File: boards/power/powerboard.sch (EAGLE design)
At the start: 55 parts, among them IC1 TPS5420, IC2 TPS5420

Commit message: Changing boards for fet and text improvements
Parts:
- R2, R4: value (none) -> 500
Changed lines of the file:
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@@
 <part name="R6" library="rcl" deviceset="R-TRIMM" device="3224W"/>
 <part name="R7" library="rcl" deviceset="R-TRIMM" device="3224W"/>
-<part name="R2" library="rcl" deviceset="R-US_" device="R3216"/>
-<part name="R4" library="rcl" deviceset="R-US_" device="R3216"/>
+<part name="R2" library="rcl" deviceset="R-US_" device="R3216" value="500"/>
+<part name="R4" library="rcl" deviceset="R-US_" device="R3216" value="500"/>
 <part name="U$2" library="40xx" deviceset="LM3488" device=""/>
 <part name="COUT" library="rcl" deviceset="CPOL-EU" device="SANYO_SMD_A5" value="56uF"/>

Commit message: New board for plugin regulator
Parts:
- removed CBP: 100nF, rcl:C-EUC0805
- removed CCOMP: 120nF, rcl:C-EUC0805
- removed CCOMP2: 510pF, rcl:C-EUC0805
- removed CIN: 22uF, rcl:C-EUC0805
- removed COUT, COUT1: 56uF, rcl:CPOL-EUSANYO_SMD_A5
- removed CRAMP: 750pF, rcl:C-EUC0805
- removed CSEP: 2.2uF, rcl:C-EUC0805
- removed LIN: 6.2uH, SparkFun-Passives:INDUCTORSRU1038
- removed LOUT: 15uH, SparkFun-Passives:INDUCTORSRU1038
- removed RBP: 20.0, rcl:R-US_R0805
- removed RCOMP: 1.47k, rcl:R-US_R0805
- removed RFADJ: 34.8k, rcl:R-US_R0805
- removed RFB1: 10k, rcl:R-US_R0805
- removed RFB2: 37.4k, rcl:R-US_R0805
- removed RRAMP: 100.0, rcl:R-US_R0805
- removed RSENSE: 0.016, rcl:R-EU_R2512
- removed U$5: P-CHANNEL20V(D-S)MOSFET, ngohara_parts:P-CHANNEL20V(D-S)MOSFET
- removed U$6: DPAK_DIODE, ngohara_parts:DPAK_DIODE
- added JP1: (no value), SparkFun-Connectors:M04LOCK
- added R10, R11, R8, R9: 0, resistor:R-EU_R0805
- added U$4: THERMAL_PAD, ngohara_parts:THERMAL_PAD
- U$2: value LM3488 -> THERMAL_PAD; device 40xx:LM3488 -> ngohara_parts:THERMAL_PAD
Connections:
- removed net 6V: COUT.+, COUT1.+, RFB2.1, U$6.C, X3.2
- removed net FB: RFB1.1, RFB2.2, U$2.FB
- removed net LINSIG: CSEP.1, LIN.2, U$5.S
- removed net LSIG: CSEP.2, LOUT.1, U$6.A
- removed net N$1: CCOMP.1, RCOMP.1
- removed net N$20: RFADJ.2, U$2.FA/SD
- removed net N$21: CRAMP.1, RRAMP.2, U$2.ISEN
- removed net N$23: U$2.DR, U$5.G
- removed net N$3: CCOMP2.1, RCOMP.2, U$2.COMP
- removed net N$9: CBP.1, RBP.1, U$2.VIN
- removed net SIG1: RRAMP.1, RSENSE.2, U$5.D
- new net 6VOUT: JP1.4, X3.2
- new net VIN: JP1.2, R10.2, R11.2, R8.2, R9.2
- net 5V: now also R10.1, R11.1
- net GND: now also JP1.3; no longer CBP.2, CCOMP.2, CCOMP2.2, CIN.2, COUT.-, COUT1.-, CRAMP.2, LOUT.2, RFADJ.1, RFB1.2, RSENSE.1, U$2.AGND, U$2.PGND
- net V_BATT: now also R8.1, R9.1; no longer CIN.1, LIN.1, RBP.2
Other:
- moved on the sheet: X3

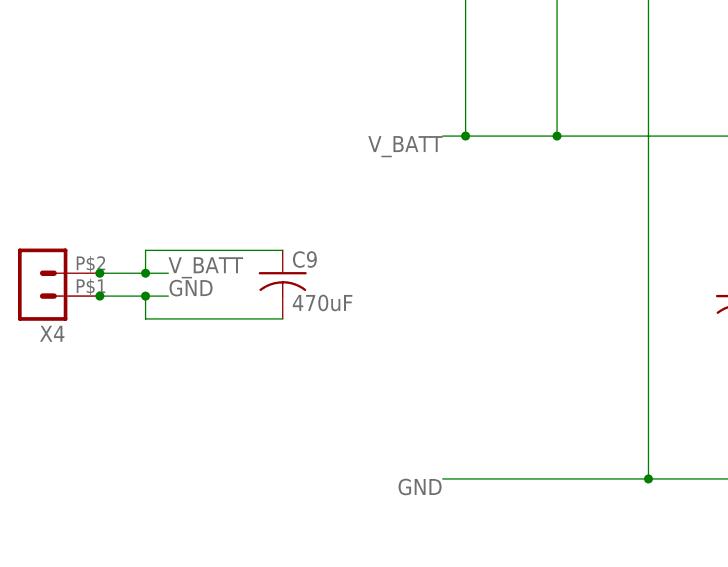
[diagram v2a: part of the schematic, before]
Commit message: Fixed 470 cap footprint
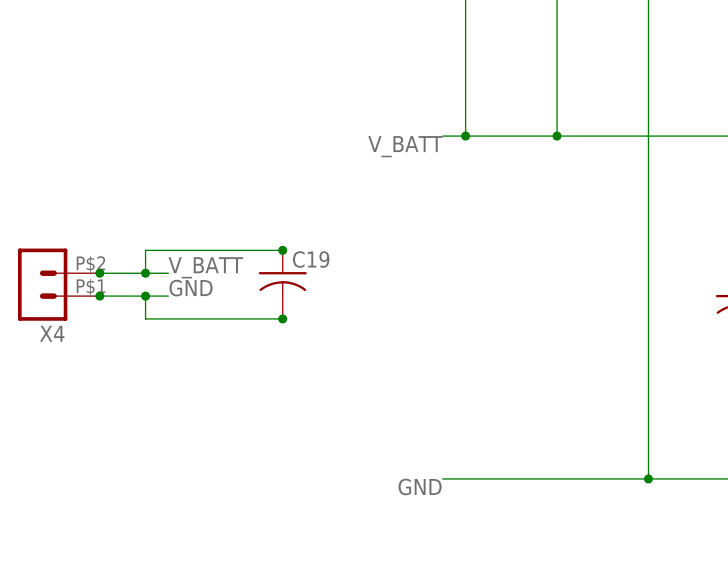
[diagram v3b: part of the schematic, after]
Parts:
- removed C9: 470uF, resistor:C-USC1812K
- added C19: (no value), custom_cap:C-USC2220K
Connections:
- net GND: now also C19.2; no longer C9.2
- net V_BATT: now also C19.1; no longer C9.1
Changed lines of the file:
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@@
 <?xml version="1.0" encoding="utf-8"?>
 <!DOCTYPE eagle SYSTEM "eagle.dtd">
-<eagle version="6.4">
+<eagle version="6.5.0">
 <drawing>
 <settings>
@@
 <part name="U$1" library="inductor-coilcraft-3" deviceset="MSS1260" device="" value="33uH"/>
 <part name="IC1" library="daniel" deviceset="TPS5420" device=""/>
-<part name="C9" library="resistor" deviceset="C-US" device="C1812K" value="470uF"/>
 <part name="C10" library="rcl" deviceset="CPOL-US" device="C/6032-28R" value="100uF"/>
 <part name="C11" library="rcl" deviceset="C-US" device="C1206K" value=".1uF"/>
@@
 <part name="U$2" library="ngohara_parts" deviceset="THERMAL_PAD" device=""/>
 <part name="U$4" library="ngohara_parts" deviceset="THERMAL_PAD" device=""/>
+<part name="C19" library="custom_cap" deviceset="C-US" device="C2220K"/>
 </parts>
 <sheets>
@@
 <instance part="U$1" gate="G$1" x="53.34" y="-20.32" rot="R90"/>
 <instance part="IC1" gate="P" x="20.32" y="-25.4"/>
-<instance part="C9" gate="G$1" x="-68.58" y="-35.56"/>
 <instance part="C10" gate="G$1" x="96.52" y="27.94"/>
 <instance part="C11" gate="G$1" x="109.22" y="27.94"/>
@@
 <instance part="U$2" gate="G$1" x="10.16" y="-99.06"/>
 <instance part="U$4" gate="G$1" x="10.16" y="-114.3"/>
+<instance part="C19" gate="G$1" x="-68.58" y="-35.56"/>
 </instances>
 <busses>
@@
 <junction x="-83.82" y="-38.1"/>
 <wire x1="-83.82" y1="-38.1" x2="-83.82" y2="-40.64" width="0.1524" layer="91"/>
-<pinref part="C9" gate="G$1" pin="2"/>
 <wire x1="-68.58" y1="-40.64" x2="-83.82" y2="-40.64" width="0.1524" layer="91"/>
 <label x="-81.28" y="-38.1" size="1.778" layer="95"/>
+<pinref part="C19" gate="G$1" pin="2"/>
+<junction x="-68.58" y="-40.64"/>
 </segment>
 <segment>
@@
 <wire x1="-81.28" y1="-35.56" x2="-83.82" y2="-35.56" width="0.1524" layer="91"/>
 <wire x1="-83.82" y1="-35.56" x2="-83.82" y2="-33.02" width="0.1524" layer="91"/>
-<pinref part="C9" gate="G$1" pin="1"/>
 <wire x1="-68.58" y1="-33.02" x2="-83.82" y2="-33.02" width="0.1524" layer="91"/>
 <label x="-81.28" y="-35.56" size="1.778" layer="95"/>
+<pinref part="C19" gate="G$1" pin="1"/>
+<junction x="-68.58" y="-33.02"/>
 </segment>
 </net>

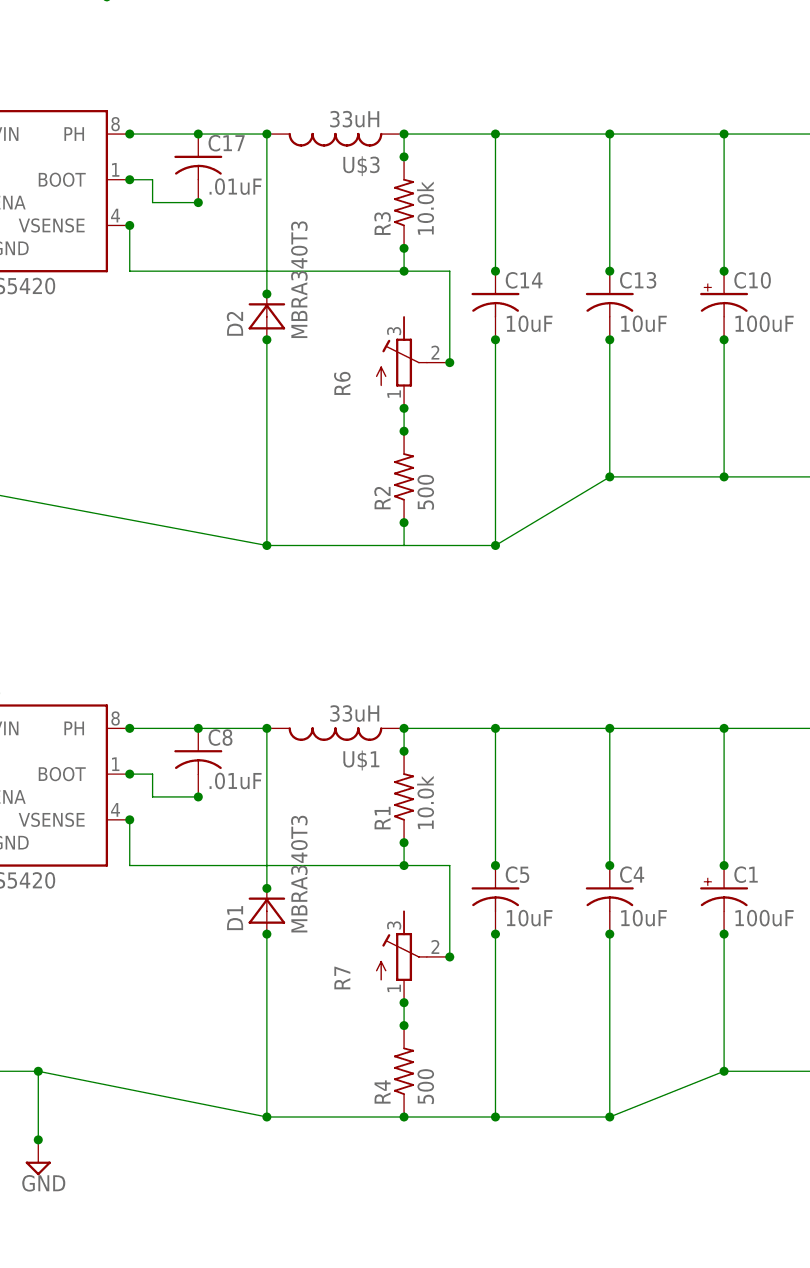
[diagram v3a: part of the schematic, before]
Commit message: changed resistors and fixed text
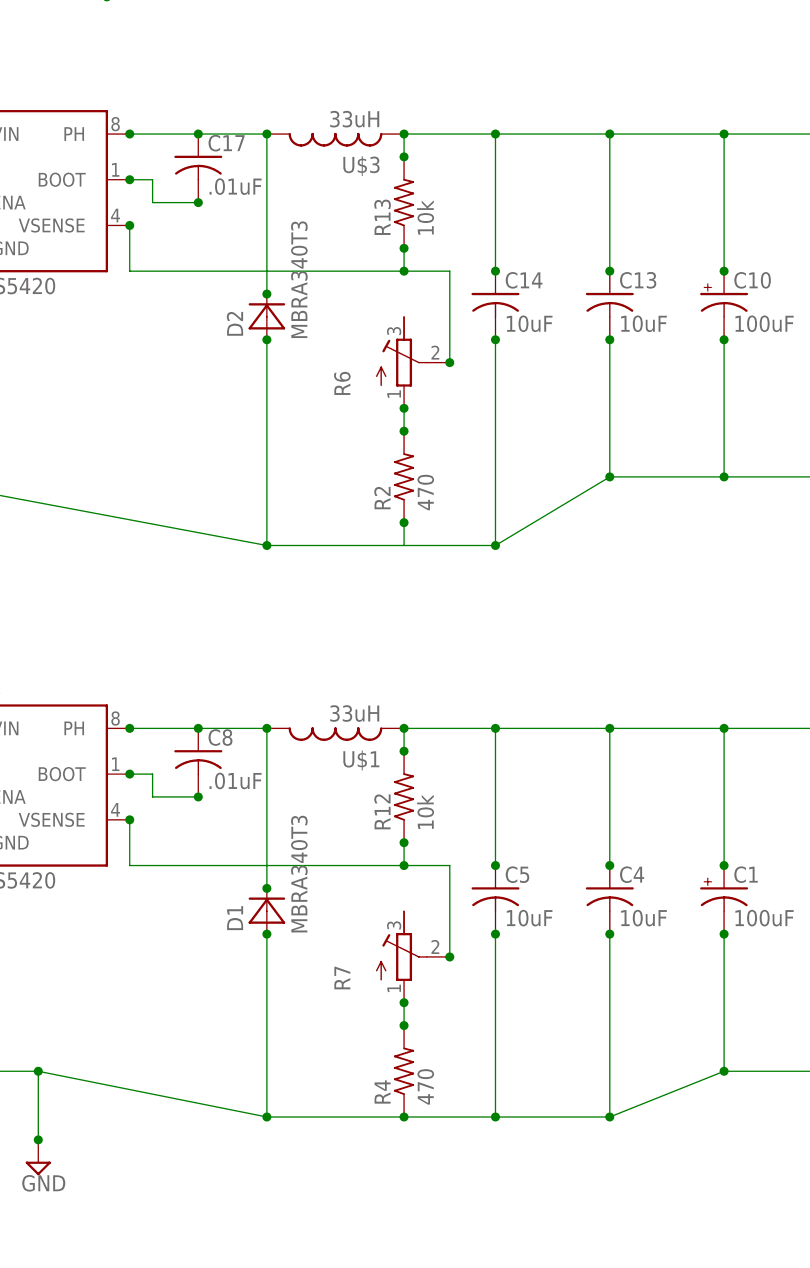
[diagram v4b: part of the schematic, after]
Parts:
- removed R1, R3: 10.0k, rcl:R-US_R3216
- added R12, R13: 10k, rcl:R-US_M0805
- R2, R4: value 500 -> 470
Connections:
- net 3_3V: now also R13.2; no longer R3.2
- net 5V: now also R12.2; no longer R1.2
- net N$12: now also R13.1; no longer R3.1
- net N$5: now also R12.1; no longer R1.1
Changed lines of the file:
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@@
 <part name="D1" library="diode" deviceset="MBRA340T3" device=""/>
 <part name="C8" library="rcl" deviceset="C-US" device="C0805K" value=".01uF"/>
-<part name="R1" library="rcl" deviceset="R-US_" device="R3216" value="10.0k"/>
 <part name="SUPPLY1" library="supply2" deviceset="GND" device=""/>
 <part name="U$1" library="inductor-coilcraft-3" deviceset="MSS1260" device="" value="33uH"/>
@@
 <part name="D2" library="diode" deviceset="MBRA340T3" device=""/>
 <part name="C17" library="rcl" deviceset="C-US" device="C0805K" value=".01uF"/>
-<part name="R3" library="rcl" deviceset="R-US_" device="R3216" value="10.0k"/>
 <part name="U$3" library="inductor-coilcraft-3" deviceset="MSS1260" device="" value="33uH"/>
 <part name="IC2" library="daniel" deviceset="TPS5420" device=""/>
@@
 <part name="R6" library="rcl" deviceset="R-TRIMM" device="3224W"/>
 <part name="R7" library="rcl" deviceset="R-TRIMM" device="3224W"/>
-<part name="R2" library="rcl" deviceset="R-US_" device="R3216" value="500"/>
-<part name="R4" library="rcl" deviceset="R-US_" device="R3216" value="500"/>
+<part name="R2" library="rcl" deviceset="R-US_" device="R3216" value="470"/>
+<part name="R4" library="rcl" deviceset="R-US_" device="R3216" value="470"/>
 <part name="SUPPLY3" library="supply2" deviceset="GND" device=""/>
 <part name="JP1" library="SparkFun-Connectors" deviceset="M04" device="LOCK"/>
@@
 <part name="U$4" library="ngohara_parts" deviceset="THERMAL_PAD" device=""/>
 <part name="C19" library="custom_cap" deviceset="C-US" device="C2220K"/>
+<part name="R12" library="rcl" deviceset="R-US_" device="M0805" value="10k"/>
+<part name="R13" library="rcl" deviceset="R-US_" device="M0805" value="10k"/>
 </parts>
 <sheets>
@@
 <instance part="D1" gate="G$1" x="45.72" y="-40.64" rot="R90"/>
 <instance part="C8" gate="G$1" x="38.1" y="-22.86"/>
-<instance part="R1" gate="G$1" x="60.96" y="-27.94" rot="R90"/>
 <instance part="SUPPLY1" gate="GND" x="20.32" y="-68.58"/>
 <instance part="U$1" gate="G$1" x="53.34" y="-20.32" rot="R90"/>
@@
 <instance part="D2" gate="G$1" x="45.72" y="25.4" rot="R90"/>
 <instance part="C17" gate="G$1" x="38.1" y="43.18"/>
-<instance part="R3" gate="G$1" x="60.96" y="38.1" rot="R90"/>
 <instance part="U$3" gate="G$1" x="53.34" y="45.72" rot="R90"/>
 <instance part="IC2" gate="P" x="20.32" y="40.64"/>
@@
 <instance part="U$4" gate="G$1" x="10.16" y="-114.3"/>
 <instance part="C19" gate="G$1" x="-68.58" y="-35.56"/>
+<instance part="R12" gate="G$1" x="60.96" y="-27.94" rot="R90"/>
+<instance part="R13" gate="G$1" x="60.96" y="38.1" rot="R90"/>
 </instances>
 <busses>
@@
 <net name="5V" class="1">
 <segment>
-<pinref part="R1" gate="G$1" pin="2"/>
 <wire x1="60.96" y1="-20.32" x2="71.12" y2="-20.32" width="0.1524" layer="91"/>
 <wire x1="71.12" y1="-20.32" x2="83.82" y2="-20.32" width="0.1524" layer="91"/>
@@
 <pinref part="C3" gate="G$1" pin="1"/>
 <wire x1="121.92" y1="-35.56" x2="121.92" y2="-24.13" width="0.1524" layer="91"/>
-<junction x="60.96" y="-22.86"/>
 <junction x="71.12" y="-20.32"/>
 <junction x="83.82" y="-20.32"/>
@@
 <pinref part="R11" gate="G$1" pin="1"/>
 <junction x="-43.18" y="-114.3"/>
+<pinref part="R12" gate="G$1" pin="2"/>
+<junction x="60.96" y="-22.86"/>
 </segment>
 </net>
@@
 <net name="N$5" class="0">
 <segment>
-<pinref part="R1" gate="G$1" pin="1"/>
 <wire x1="60.96" y1="-33.02" x2="60.96" y2="-35.56" width="0.1524" layer="91"/>
 <wire x1="30.48" y1="-30.48" x2="30.48" y2="-35.56" width="0.1524" layer="91"/>
 <wire x1="30.48" y1="-35.56" x2="60.96" y2="-35.56" width="0.1524" layer="91"/>
-<junction x="60.96" y="-33.02"/>
 <pinref part="IC1" gate="P" pin="VSENSE"/>
 <junction x="30.48" y="-30.48"/>
@@
 <wire x1="66.04" y1="-35.56" x2="66.04" y2="-45.72" width="0.1524" layer="91"/>
 <junction x="60.96" y="-35.56"/>
+<pinref part="R12" gate="G$1" pin="1"/>
+<junction x="60.96" y="-33.02"/>
 </segment>
 </net>
@@
 <net name="3_3V" class="1">
 <segment>
-<pinref part="R3" gate="G$1" pin="2"/>
 <wire x1="60.96" y1="45.72" x2="71.12" y2="45.72" width="0.1524" layer="91"/>
 <wire x1="71.12" y1="45.72" x2="83.82" y2="45.72" width="0.1524" layer="91"/>
@@
 <pinref part="C12" gate="G$1" pin="1"/>
 <wire x1="121.92" y1="30.48" x2="121.92" y2="45.72" width="0.1524" layer="91"/>
-<junction x="60.96" y="43.18"/>
 <junction x="71.12" y="45.72"/>
 <junction x="83.82" y="45.72"/>
@@
 <junction x="154.94" y="45.72"/>
 <junction x="154.94" y="27.94"/>
+<pinref part="R13" gate="G$1" pin="2"/>
+<junction x="60.96" y="43.18"/>
 </segment>
 </net>
@@
 <net name="N$12" class="0">
 <segment>
-<pinref part="R3" gate="G$1" pin="1"/>
 <wire x1="60.96" y1="33.02" x2="60.96" y2="30.48" width="0.1524" layer="91"/>
 <wire x1="30.48" y1="35.56" x2="30.48" y2="30.48" width="0.1524" layer="91"/>
 <wire x1="30.48" y1="30.48" x2="60.96" y2="30.48" width="0.1524" layer="91"/>
-<junction x="60.96" y="33.02"/>
 <pinref part="IC2" gate="P" pin="VSENSE"/>
 <junction x="30.48" y="35.56"/>
@@
 <junction x="66.04" y="20.32"/>
 <junction x="60.96" y="30.48"/>
-</segment>
-</net>
+<pinref part="R13" gate="G$1" pin="1"/>
+<junction x="60.96" y="33.02"/>
+</segment>
+</net>
